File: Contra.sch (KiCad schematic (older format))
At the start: 103 parts, among them P1 Pad, P2 Pad, P3 Pad, P4 Pad, SW1 SW_PUSH, U1 ProMicro

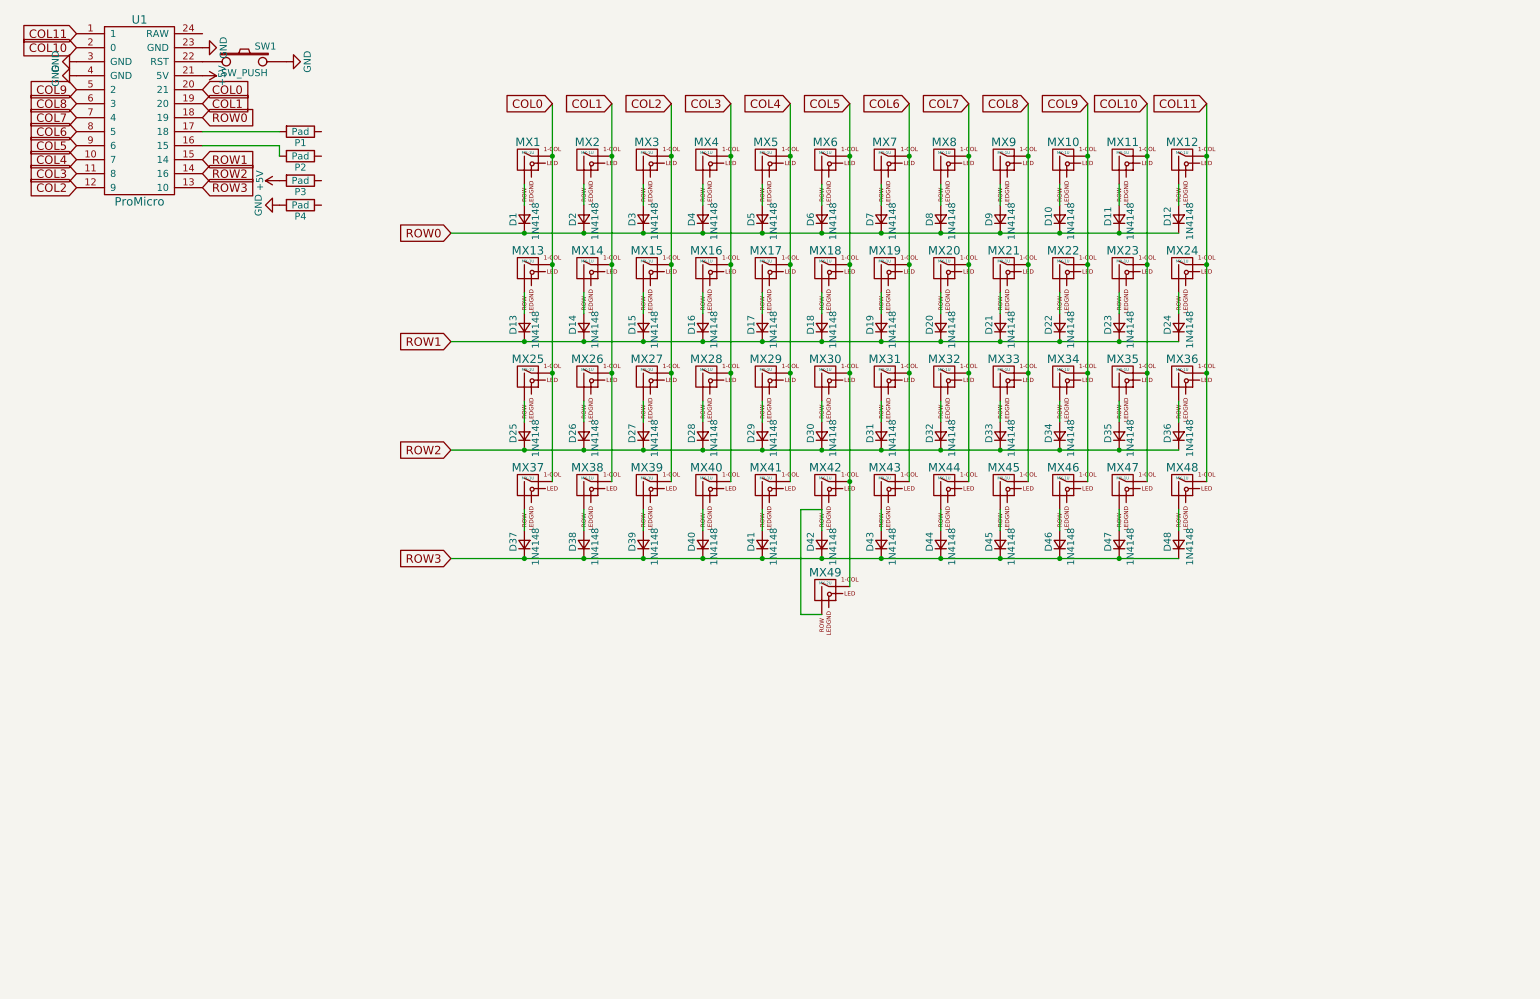
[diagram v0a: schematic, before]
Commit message: Rename project files
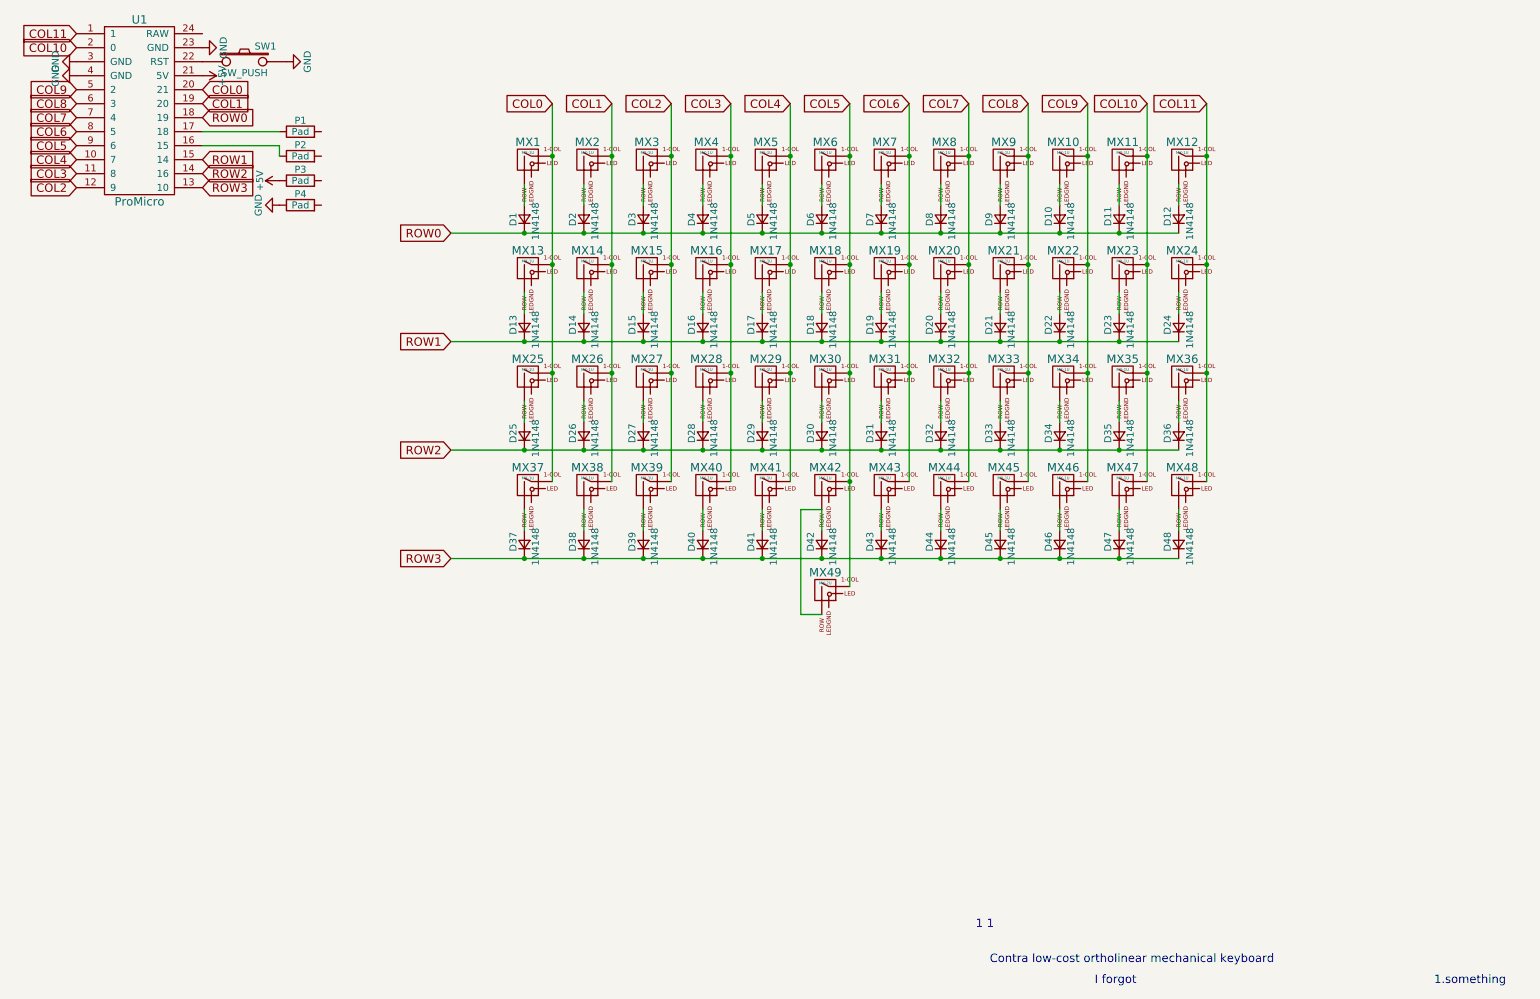
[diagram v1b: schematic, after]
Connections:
- net +5V: now also P3.1; no longer P3.2
- net GND: now also P4.1; no longer P4.2
- net at U1.16 (15): now also P2.1; no longer P2.2
- net at U1.17 (18): now also P1.1; no longer P1.2
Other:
- note added: "1 1\n"
- note added: "1.something\n"
- note added: "Contra low-cost ortholinear mechanical keyboard\n"
- note added: "I forgot"
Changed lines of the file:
@@
 LIBS:Molex-0548190589
 LIBS:MX_Alps_Hybrids
-LIBS:Danck-cache
+LIBS:Contra-cache
 EELAYER 25 0
 EELAYER END
@@
 F 3 "" H 2450 1550 50  0001 C CNN
 	1    2450 1550
-	0    1    1    0
+	0    -1   -1   0
 $EndComp
 $Comp
@@
 F 3 "" H 2450 1725 50  0001 C CNN
 	1    2450 1725
-	0    1    1    0
+	0    -1   -1   0
 $EndComp
 Wire Wire Line
@@
 F 3 "" H 2450 1900 50  0001 C CNN
 	1    2450 1900
-	0    1    1    0
-$EndComp
-$Comp
-L +5V #PWR?
+	0    -1   -1   0
+$EndComp
+$Comp
+L +5V #PWR06
 U 1 1 5A323A72
 P 2300 1900
-F 0 "#PWR?" H 2300 1750 50  0001 C CNN
+F 0 "#PWR06" H 2300 1750 50  0001 C CNN
 F 1 "+5V" H 2300 2040 50  0000 C CNN
 F 2 "" H 2300 1900 50  0001 C CNN
@@
 F 3 "" H 2450 2075 50  0001 C CNN
 	1    2450 2075
-	0    1    1    0
-$EndComp
-$Comp
-L GND #PWR?
+	0    -1   -1   0
+$EndComp
+$Comp
+L GND #PWR07
 U 1 1 5A323E4A
 P 2300 2075
-F 0 "#PWR?" H 2300 1825 50  0001 C CNN
+F 0 "#PWR07" H 2300 1825 50  0001 C CNN
 F 1 "GND" H 2300 1925 50  0000 C CNN
 F 2 "" H 2300 2075 50  0001 C CNN
@@
 	0    1    1    0
 $EndComp
+Text Notes 7375 7500 0    60   ~ 0
+Contra low-cost ortholinear mechanical keyboard\n
+Text Notes 7275 7250 0    60   ~ 0
+1 1\n
+Text Notes 8125 7650 0    60   ~ 0
+I forgot
+Text Notes 10550 7650 0    60   ~ 0
+1.something\n
 $EndSCHEMATC

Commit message: Update locallib
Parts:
- D1, D10, D11, D12, D13, D14, D15, D16, D17, D18, D19, D2, D20, D21, D22, D23, D24, D25, D26, D27, D28, D29, D3, D30, D31, D32, D33, D34, D35, D36, D37, D38, D39, D4, D40, D41, D42, D43, D44, D45, D46, D47, D48, D5, D6, D7, D8, D9: symbol D_Small -> Device:D_Small
- MX1, MX10, MX11, MX12, MX13, MX14, MX15, MX16, MX17, MX18, MX19, MX2, MX20, MX21, MX22, MX23, MX24, MX25, MX26, MX27, MX28, MX29, MX3, MX30, MX31, MX32, MX33, MX34, MX35, MX36, MX37, MX38, MX39, MX4, MX40, MX41, MX42, MX43, MX44, MX45, MX46, MX47, MX48, MX5, MX6, MX7, MX8, MX9: symbol MX-1U -> MX_Alps_Hybrids:MX-1U
- MX49: symbol MX-2U -> MX_Alps_Hybrids:MX-2U
- P1, P2, P3, P4: symbol R -> Device:R
- SW1: symbol SW_PUSH -> keyboard_parts:SW_PUSH
- U1: symbol ProMicro -> josh:ProMicro

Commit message: Make diodes double sided
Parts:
- D1, D10, D11, D12, D13, D14, D15, D16, D17, D18, D19, D2, D20, D21, D22, D23, D24, D25, D26, D27, D28, D29, D3, D30, D31, D32, D33, D34, D35, D36, D37, D38, D39, D4, D40, D41, D42, D43, D44, D45, D46, D47, D48, D5, D6, D7, D8, D9: footprint Diodes_THT:D_DO-35_SOD27_P7.62mm_Horizontal -> locallib:D_DO-35_SOD27_P7.62mm_Horizontal-DoubleSided

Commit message: Update gerbers
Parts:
- removed P1, P2, P3, P4: Pad, locallib:mountinghole, symbol Device:R
- added J1: Conn_01x04, Pin_Headers:Pin_Header_Straight_1x04_Pitch2.54mm, symbol Connector_Generic:Conn_01x04
- SW1: footprint Molex-0548190589:PushButton_6x6mm_TH -> Molex-0548190589:PushButton_6x6mm_TH_Pretty
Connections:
- net labels added: PIN15, PIN18
- wire segments 151 -> 148
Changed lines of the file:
@@
 F 0 "SW1" H 2200 1160 50  0000 C CNN
 F 1 "SW_PUSH" H 2050 970 50  0000 C CNN
-F 2 "Molex-0548190589:PushButton_6x6mm_TH" H 2050 1050 60  0001 C CNN
+F 2 "Molex-0548190589:PushButton_6x6mm_TH_Pretty" H 2050 1050 60  0001 C CNN
 F 3 "" H 2050 1050 60  0000 C CNN
 	1    2050 1050
@@
 ROW0
 $Comp
-L Device:R P1
-U 1 1 5A322ABB
-P 2450 1550
-F 0 "P1" V 2530 1550 50  0000 C CNN
-F 1 "Pad" V 2450 1550 50  0000 C CNN
-F 2 "locallib:mountinghole" V 2380 1550 50  0001 C CNN
-F 3 "" H 2450 1550 50  0001 C CNN
-	1    2450 1550
-	0    -1   -1   0
-$EndComp
-$Comp
-L Device:R P2
-U 1 1 5A322DD0
-P 2450 1725
-F 0 "P2" V 2530 1725 50  0000 C CNN
-F 1 "Pad" V 2450 1725 50  0000 C CNN
-F 2 "locallib:mountinghole" V 2380 1725 50  0001 C CNN
-F 3 "" H 2450 1725 50  0001 C CNN
-	1    2450 1725
-	0    -1   -1   0
-$EndComp
-Wire Wire Line
-	2300 1550 1750 1550
-Wire Wire Line
-	1750 1650 2300 1650
-Wire Wire Line
-	2300 1650 2300 1725
-$Comp
-L Device:R P3
-U 1 1 5A323624
-P 2450 1900
-F 0 "P3" V 2530 1900 50  0000 C CNN
-F 1 "Pad" V 2450 1900 50  0000 C CNN
-F 2 "locallib:mountinghole" V 2380 1900 50  0001 C CNN
-F 3 "" H 2450 1900 50  0001 C CNN
-	1    2450 1900
-	0    -1   -1   0
-$EndComp
-$Comp
 L power:+5V #PWR06
 U 1 1 5A323A72
-P 2300 1900
-F 0 "#PWR06" H 2300 1750 50  0001 C CNN
-F 1 "+5V" H 2300 2040 50  0000 C CNN
-F 2 "" H 2300 1900 50  0001 C CNN
-F 3 "" H 2300 1900 50  0001 C CNN
-	1    2300 1900
-	0    -1   -1   0
-$EndComp
-$Comp
-L Device:R P4
-U 1 1 5A323BB6
-P 2450 2075
-F 0 "P4" V 2530 2075 50  0000 C CNN
-F 1 "Pad" V 2450 2075 50  0000 C CNN
-F 2 "locallib:mountinghole" V 2380 2075 50  0001 C CNN
-F 3 "" H 2450 2075 50  0001 C CNN
-	1    2450 2075
+P 1825 3125
+F 0 "#PWR06" H 1825 2975 50  0001 C CNN
+F 1 "+5V" H 1825 3265 50  0000 C CNN
+F 2 "" H 1825 3125 50  0001 C CNN
+F 3 "" H 1825 3125 50  0001 C CNN
+	1    1825 3125
 	0    -1   -1   0
 $EndComp
@@
 L power:GND #PWR07
 U 1 1 5A323E4A
-P 2300 2075
-F 0 "#PWR07" H 2300 1825 50  0001 C CNN
-F 1 "GND" H 2300 1925 50  0000 C CNN
-F 2 "" H 2300 2075 50  0001 C CNN
-F 3 "" H 2300 2075 50  0001 C CNN
-	1    2300 2075
+P 1825 2825
+F 0 "#PWR07" H 1825 2575 50  0001 C CNN
+F 1 "GND" H 1825 2675 50  0000 C CNN
+F 2 "" H 1825 2825 50  0001 C CNN
+F 3 "" H 1825 2825 50  0001 C CNN
+	1    1825 2825
 	0    1    1    0
 $EndComp
@@
 Wire Wire Line
 	6375 4050 6375 4800
+$Comp
+L Connector_Generic:Conn_01x04 J1
+U 1 1 5BFDE52B
+P 2025 2925
+F 0 "J1" H 2105 2917 50  0000 L CNN
+F 1 "Conn_01x04" H 2105 2826 50  0000 L CNN
+F 2 "Pin_Headers:Pin_Header_Straight_1x04_Pitch2.54mm" H 2025 2925 50  0001 C CNN
+F 3 "~" H 2025 2925 50  0001 C CNN
+	1    2025 2925
+	1    0    0    -1
+$EndComp
+Text GLabel 1750 1550 2    50   Input ~ 0
+PIN18
+Text GLabel 1750 1650 2    50   Input ~ 0
+PIN15
+Text GLabel 1825 2925 0    50   Input ~ 0
+PIN15
+Text GLabel 1825 3025 0    50   Input ~ 0
+PIN18
 $EndSCHEMATC
